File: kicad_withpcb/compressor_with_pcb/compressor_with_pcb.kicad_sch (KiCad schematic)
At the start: 166 parts, among them J1 EDA 306, Q1 BC549C, Q2 BC549C, Q3 BC549C, Q4 BC549C, Q5 BC549C, Q6 BC549C, Q7 BC549C, Q8 BC549C, Q9 BC549C, SW1 BYPASS, SW2 INT/EXT, SW3 HPF DEFEAT, SW4 LINK, U1 NE5532, U10 LM3915, U2 NE5532, U3 NE5532, U4 TL072, U5 NE5532, U6 NE5532, U7 NE5532, U9 LM3914

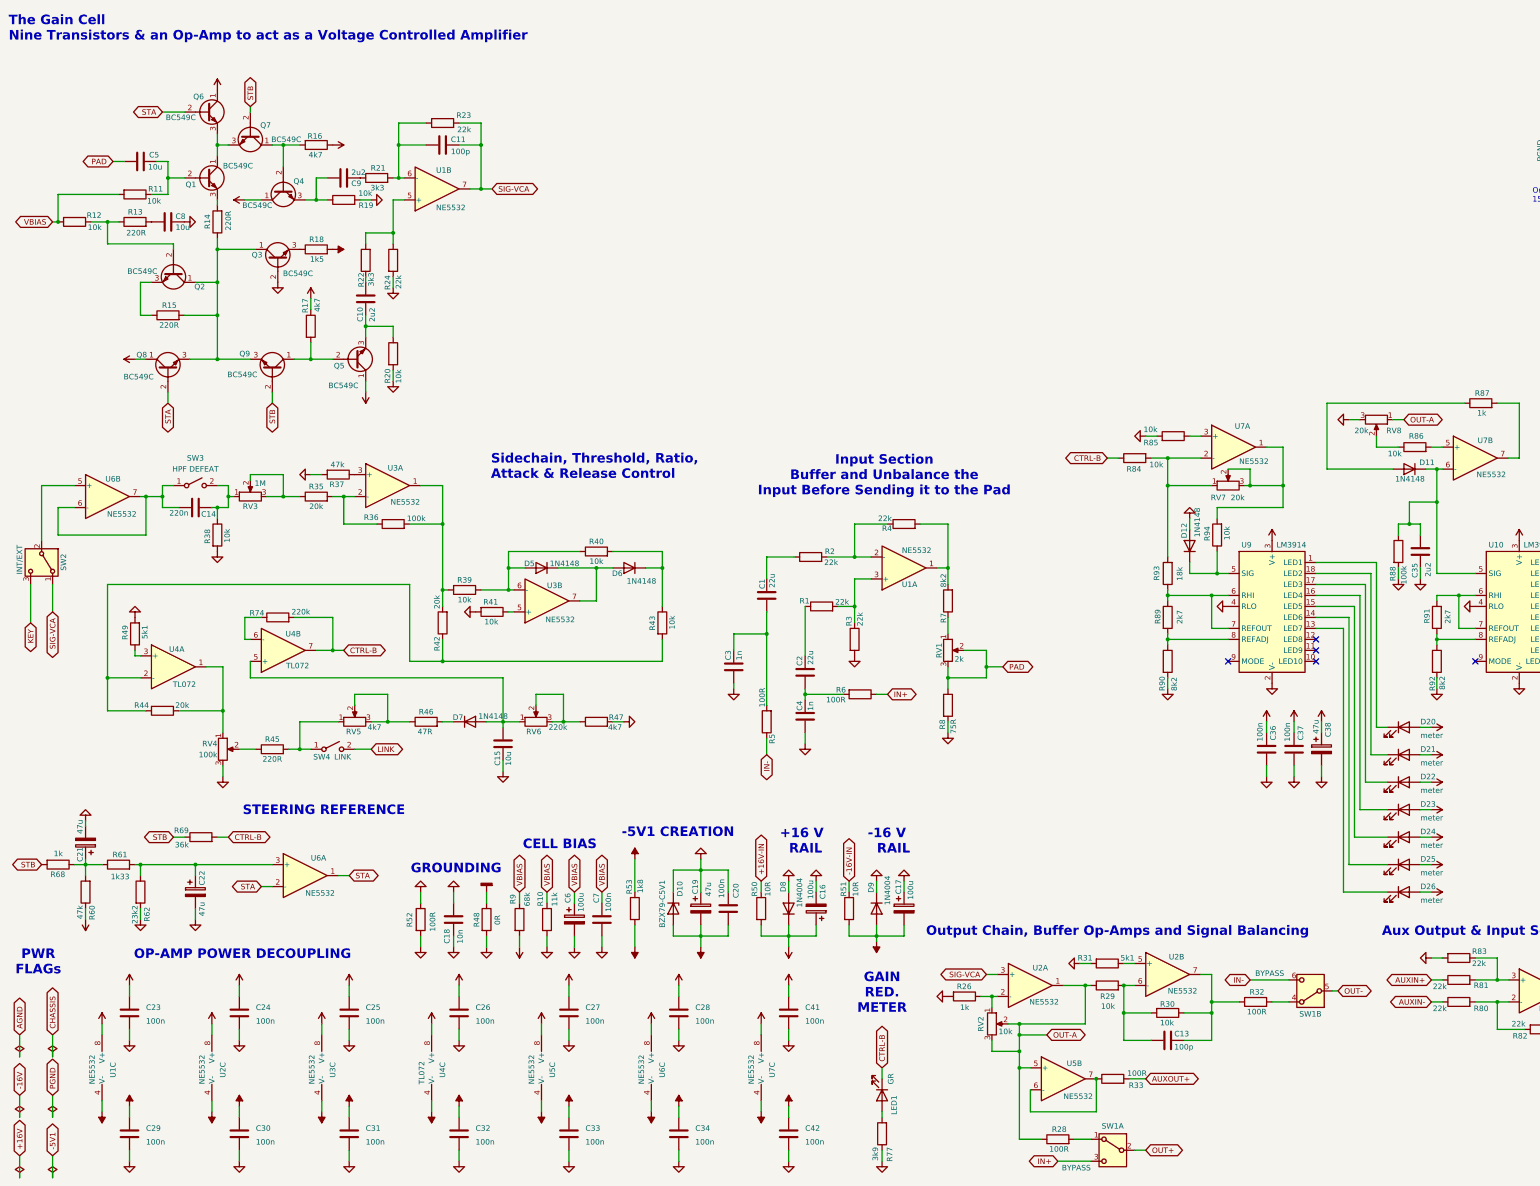
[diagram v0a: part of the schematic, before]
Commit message: Move panel controls and meters to a front board
Pots, switches and both meters now sit on a separate front board, as the
faceplate fit guide recommends. They stay drawn in the schematic but are
excluded from this board and its BOM. J2 (2x15 IDC) carries the 24 signals
that cross, with ground between the audio pairs.

Front edge set back 24 mm to clear the front board, and the card guide
keep-outs are now 3 mm on both layers.

Co-Authored-By: Claude Opus 5.5 (1M context) <noreply@anthropic.com>
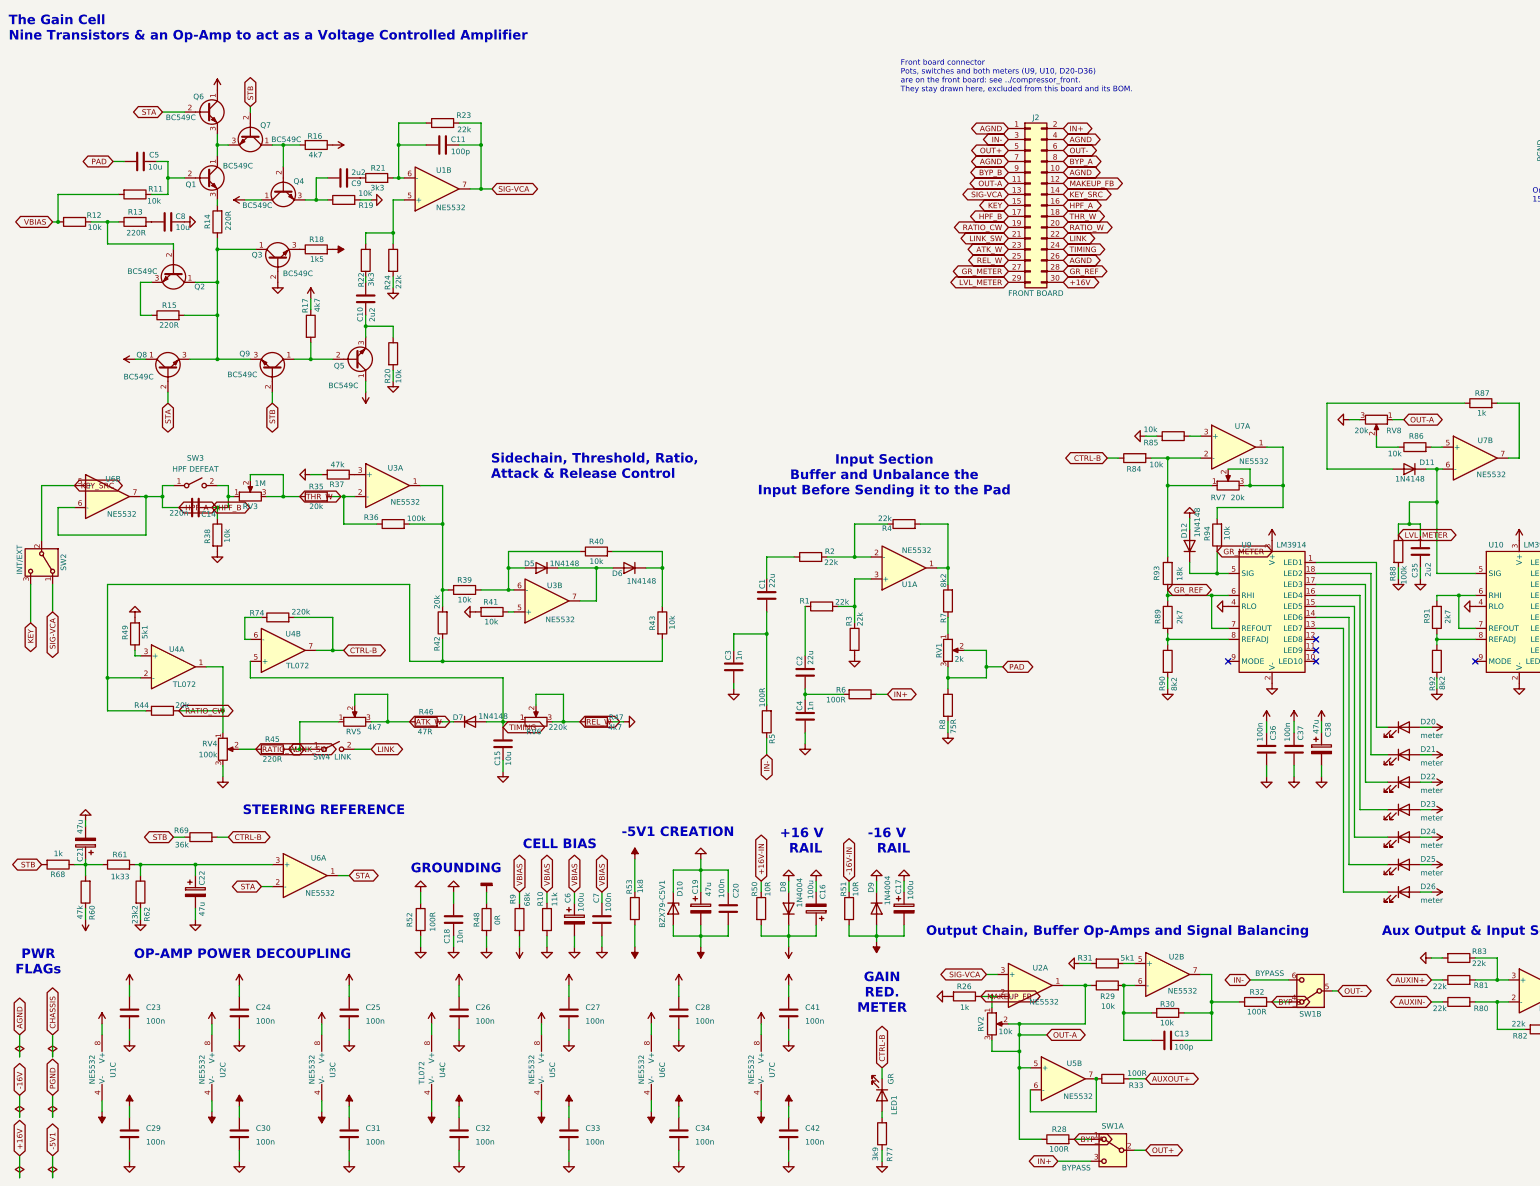
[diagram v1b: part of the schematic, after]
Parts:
- added J2: FRONT BOARD, Connector_IDC:IDC-Header_2x15_P2.54mm_Vertical, symbol Connector_Generic:Conn_02x15_Odd_Even
- C36, C37, C38, D20, D21, D22, D23, D24, D25, D26, D30, D31, D32, D33, D34, D35, D36, R89, R90, R91, R92, RV2, RV3, RV4, RV5, RV6, SW1, SW2, SW3, SW4, U10, U9: now left out of the parts list
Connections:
- net +16V: now also J2.30 (Pin_30)
- net AGND: now also J2.1 (Pin_1), J2.10 (Pin_10), J2.26 (Pin_26), J2.4 (Pin_4), J2.7 (Pin_7)
- net IN+: now also J2.2 (Pin_2)
- net IN-: now also J2.3 (Pin_3)
- net KEY: now also J2.15 (Pin_15)
- net LINK: now also J2.22 (Pin_22)
- net OUT+: now also J2.5 (Pin_5)
- net OUT-: now also J2.6 (Pin_6)
- net OUT-A: now also J2.11 (Pin_11)
- net SIG-VCA: now also J2.13 (Pin_13)
- net TIMING: now reaches C15.1, D7.2 (A), RV6.1, U4.5 (+)
- net TIMING: now also J2.24 (Pin_24)
- net REL_W: now reaches R47.1, RV6.2, RV6.3
- net REL_W: now also J2.25 (Pin_25)
- net LINK_SW: now reaches R45.2, RV5.1, SW4.1 (A)
- net LINK_SW: now also J2.21 (Pin_21)
- net LVL_METER: now reaches C35.1, D11.1 (K), R88.1, U10.5 (SIG), U7.6 (-)
- net LVL_METER: now also J2.29 (Pin_29)
- net GR_METER: now reaches D12.1 (K), R94.1, U9.5 (SIG)
- net GR_METER: now also J2.27 (Pin_27)
- net GR_REF: now reaches R89.1, R93.1, U9.6 (RHI), U9.7 (REFOUT)
- net GR_REF: now also J2.28 (Pin_28)
- net THR_W: now reaches R35.1, RV3.2, RV3.3
- net THR_W: now also J2.18 (Pin_18)
- net RATIO_CW: now reaches R44.1, RV4.1, U4.1
- net RATIO_CW: now also J2.19 (Pin_19)
- net HPF_A: now reaches C14.1, SW3.1 (A), U6.6 (-), U6.7
- net HPF_A: now also J2.16 (Pin_16)
- net HPF_B: now reaches C14.2, R38.1, RV3.1, SW3.2 (B)
- net HPF_B: now also J2.17 (Pin_17)
- net KEY_SRC: now reaches SW2.2 (B), U6.5 (+)
- net KEY_SRC: now also J2.14 (Pin_14)
- net RATIO_W: now reaches R45.1, RV4.2
- net RATIO_W: now also J2.20 (Pin_20)
- net ATK_W: now reaches R46.1, RV5.2, RV5.3
- net ATK_W: now also J2.23 (Pin_23)
- net BYP_A: now reaches R28.2, SW1.1 (A)
- net BYP_A: now also J2.8 (Pin_8)
- net MAKEUP_FB: now reaches R26.1, RV2.1, U2.2 (-)
- net MAKEUP_FB: now also J2.12 (Pin_12)
- net BYP_B: now reaches R32.2, SW1.4 (A)
- net BYP_B: now also J2.9 (Pin_9)
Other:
- note added: "Front board connector Pots, switches and both meters (U9, U10, D20-D36) are on the front board: see ../compressor_front. They stay drawn here, excluded from this board and its BOM."
